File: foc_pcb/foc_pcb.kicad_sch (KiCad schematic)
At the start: 67 parts, among them IC1 AS5600-ASOT, J1 USB_C_Receptacle_USB2.0, J10 Conn_02x03_Top_Bottom, J11 Conn_01x03, J12 USB4105-GF-A, J2 Conn_01x03, J3 Conn_01x03, J4 Conn_01x04, J5 XT60PW-M, J6 XT60PW-M, J7 Conn_01x02, J8 Conn_01x02, J9 Conn_01x02, SW1 SW_Push, U1 DRV8313PWPR, U2 ATMEGA328P-AU, U3 BSS138-7-F, U4 BSS138-7-F, U5 CH340C, Y1 ABM3-16MHZ

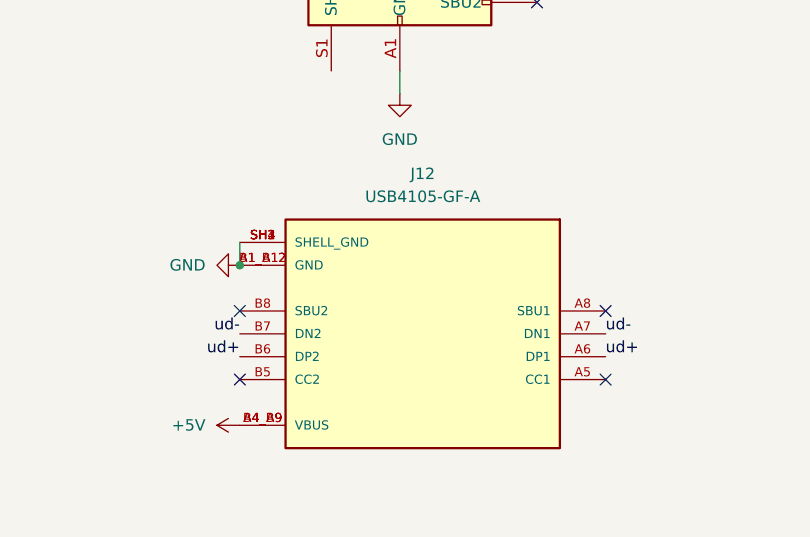
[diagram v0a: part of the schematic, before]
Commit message: reverted to old usb, pray to jlc gods
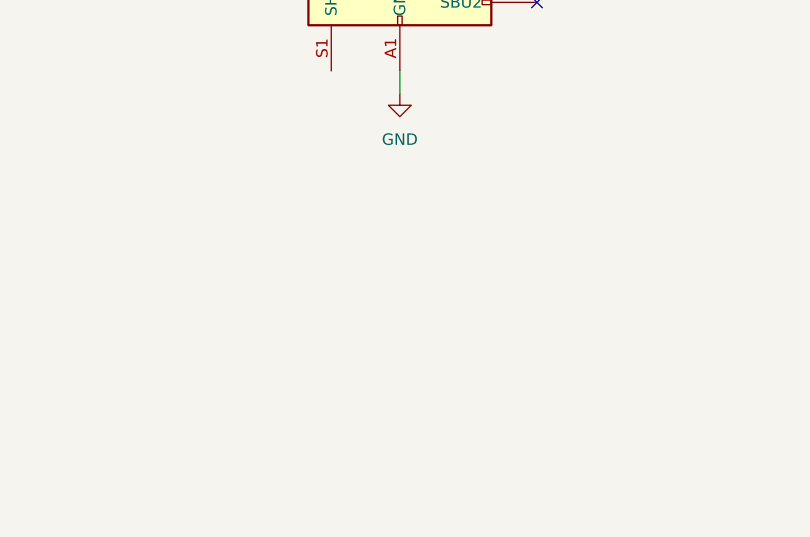
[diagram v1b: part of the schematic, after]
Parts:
- removed J12: USB4105-GF-A, USB4105-GF-A:GCT_USB4105-GF-A, symbol USB4105-GF-A:USB4105-GF-A
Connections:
- no-connect marks 14 -> 10

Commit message: board v1 done, to be ordered soon
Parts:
- removed C5: 1uF, Capacitor_SMD:C_0603_1608Metric, symbol Device:C_Polarized_US
- removed J1: USB_C_Receptacle_USB2.0, Connector_USB:USB_C_Receptacle_G-Switch_GT-USB-7010ASV, symbol Connector:USB_C_Receptacle_USB2.0
- added H10, H11, H12, H9: boardMount, MountingHole:MountingHole_3.2mm_M3, symbol Mechanical:MountingHole
- added J1: Conn_01x03, Connector_PinHeader_2.54mm:PinHeader_1x03_P2.54mm_Vertical, symbol Connector_Generic:Conn_01x03
- added J12: 10118193-0001LF, usbMicroB:AMPHENOL_10118193-0001LF, symbol 10118193-0001LF:10118193-0001LF
- C4: symbol Device:C_Polarized_US -> Device:C
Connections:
- net +5V: now also J12.1 (VUSB)
- net GND: now also J1.3 (Pin_3), J12.5 (GND)
- net uRX: now also J1.1 (Pin_1)
- net uTX: now also J1.2 (Pin_2)
- net ud+: now also J12.3 (D+)
- net ud-: now also J12.2 (D-)
- no-connect marks 10 -> 12

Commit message: readme updated
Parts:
- D1: value 19-213/Y2C-CQ2R2L/3T(CY) -> 150060RS75000
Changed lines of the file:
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@@
 			)
 		)
-		(property "Value" "19-213/Y2C-CQ2R2L/3T(CY)"
-			(at 176.53 107.95 0)
+		(property "Value" "150060RS75000"
+			(at 168.148 107.95 0)
 			(effects
 				(font

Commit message: V2 redesign done, needs review
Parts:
- removed D1: 150060RS75000, simpleFOC_led:LED0603-RD-YELLOW, symbol Device:LED
- removed D2: 1N5819HW-7-F, 1N5819HW-7-F:SOD3715X145N, symbol 1N5819HW-7-F:1N5819HW-7-F
- removed D3: LED, KT-0603R:LED0603-RD, symbol Device:LED
- removed H10, H11, H12, H9: boardMount, MountingHole:MountingHole_3.2mm_M3, symbol Mechanical:MountingHole
- removed H5, H6, H7, H8: motorMount, MountingHole:MountingHole_3.2mm_M3, symbol Mechanical:MountingHole
- removed J1, J11, J2: Conn_01x03, Connector_PinHeader_2.54mm:PinHeader_1x03_P2.54mm_Vertical, symbol Connector_Generic:Conn_01x03
- removed J4: Conn_01x04, Connector_PinHeader_2.54mm:PinHeader_1x04_P2.54mm_Vertical, symbol Connector_Generic:Conn_01x04
- removed J7: Conn_01x02, Connector_PinHeader_2.54mm:PinHeader_1x02_P2.54mm_Vertical, symbol Connector_Generic:Conn_01x02
- added D1: 1N5819HW-7-F, 1N5819HW-7-F:SOD3715X145N, symbol 1N5819HW-7-F:1N5819HW-7-F
- added J1: MPU6050, Connector_PinHeader_2.54mm:PinHeader_1x08_P2.54mm_Vertical, symbol Connector_Generic:Conn_01x08
- added U6: ~, XIAO-ESP32S3:MOUDLE14P-SMD-2.54-21X17.8MM, symbol XIAO-ESP32S3:MOUDLE-SEEEDUINO-XIAO-ESP32S3-SMD
- added U7: BSS138-7-F, BSS138-7-F:SOT95P240X110-3N, symbol BSS138-7-F:BSS138-7-F
- C11: value VT1V101M-CRE77 -> UWT1V101MCL1GS; footprint VT1V101M-CRE77:CAP-SMD_BD6.3-L6.6-W6.6-FD -> UWT1V101MCL1GS:PCAP_6.3x7.7-ELECT_NCA-L
- D5: footprint KT-0603R:LED0603-RD -> LED_SMD:LED_0603_1608Metric
- IC1: Description_1 (none) -> Hall Effect Sensor Angle External Magnet, Not Included Gull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
- J5, J6: Description_1 (none) -> Socket, DC supply, male, PIN: 2
- R4, R8: value 1k -> 10k
- U2: footprint ATMEGA328P-AU-NEW:QFP80P900X900X120-32N -> ATMEGA328P-AU:QFP80P900X900X120-32N
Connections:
- net 3vin is gone; now on net +3.3V: R15.1, R17.1, U3.1 (G), U4.1 (G)
- net aRX2 is gone; now on net GND: U2.14 (PB2)
- net +3.3V: now also R4.1, J1.1 (Pin_1), U7.1 (G)
- net +5V: now also R8.1, U5.4 (V3), VR1.2 (OUTPUT), D1.C; no longer U5.16 (VCC)
- net GND: now also J1.2 (Pin_2), U6.13 (GND)
- net VCC: no longer R4.1
- net miso: now also R18.2, U4.3 (D)
- net mosi: now also R16.2, U3.3 (D)
- net sck: now also U7.3 (D)
- net gpio_1: now reaches U2.23 (PC0)
- net gpio_2: now reaches U2.24 (PC1)
- net at C10.1, C12.2: now also U5.16 (VCC); no longer U5.4 (V3)
- net esp_sck: now reaches R4.2
- net esp_sck: now also U6.9 (PA7_A8_D8_SCK), U7.2 (S)
- removed net aRX1: R16.2, U2.12 (PB0), U3.3 (D)
- removed net aTX1: R18.2, U2.13 (PB1), U4.3 (D)
- net aTX2: no longer names the net of U2.32 (PD2)
- net escl renamed scl
- net esda renamed sda
- net lvRX renamed esp_mosi
- net esp_mosi: now also U6.11 (PA6_A10_D10_MOSI)
- net lvTX renamed esp_miso
- net esp_miso: now also U6.10 (PA5_A9_D9_MISO)
- new net: D1.A, U6.14 (5V)
- new net esp_scl_0: U6.4 (PA11_A3_D3)
- new net esp_scl_1: J1.3 (Pin_3), U6.6 (PA9_A5_D5_SCL)
- new net esp_sda_0: U6.3 (PA10_A2_D2)
- new net esp_sda_1: J1.4 (Pin_4), U6.5 (PA8_A4_D4_SDA)
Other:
- moved on the sheet: C1, C10, C11, C12, C13, C14, C16, C17, C2, C3, C4, C6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

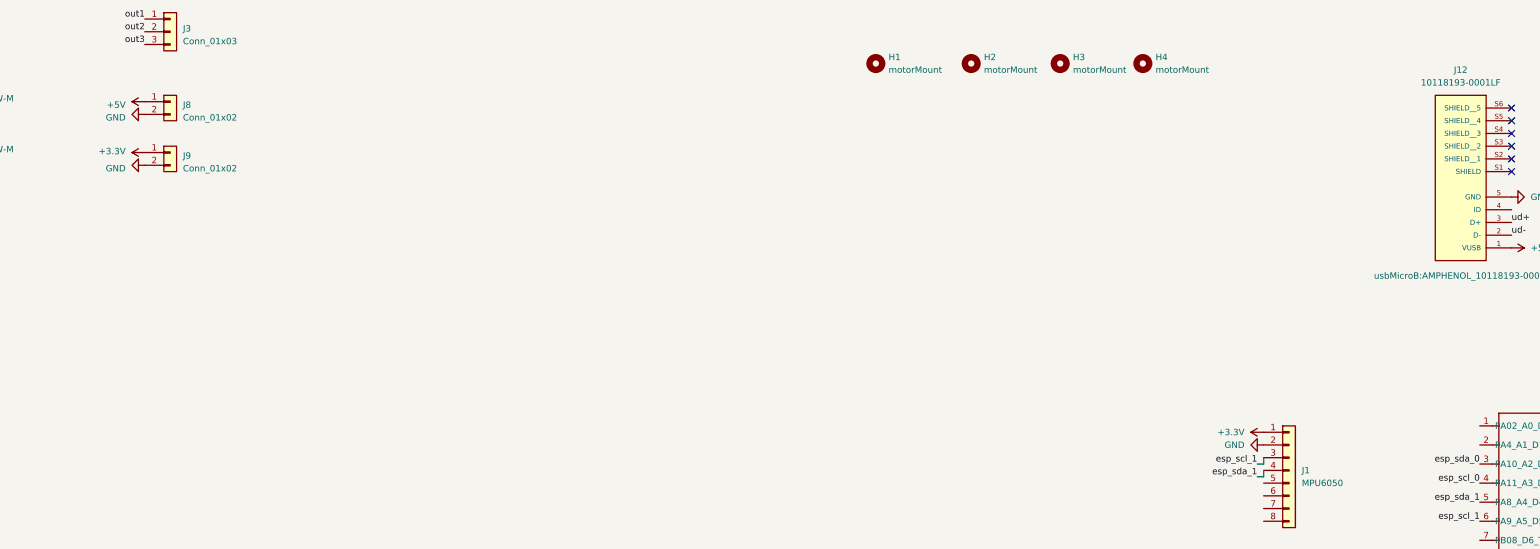
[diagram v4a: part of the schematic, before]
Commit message: compacted layout, finished V2
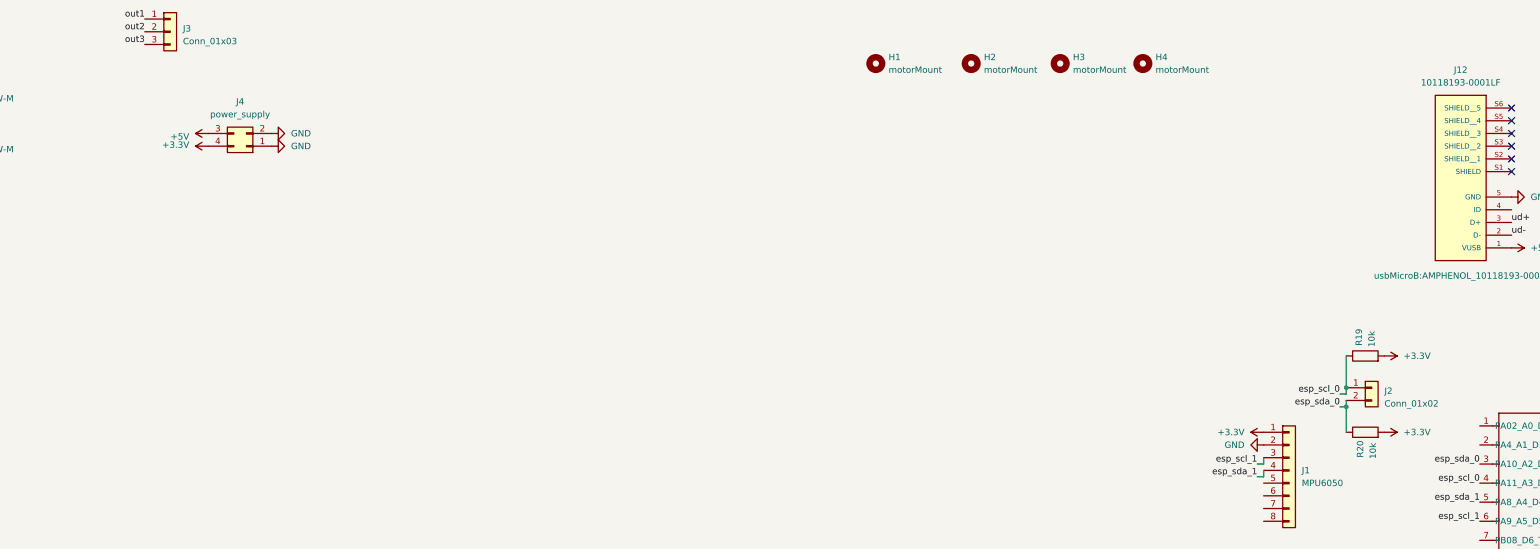
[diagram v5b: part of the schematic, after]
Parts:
- removed J8, J9: Conn_01x02, Connector_PinHeader_2.54mm:PinHeader_1x02_P2.54mm_Vertical, symbol Connector_Generic:Conn_01x02
- added J2: Conn_01x02, Connector_PinHeader_2.54mm:PinHeader_1x02_P2.54mm_Vertical, symbol Connector_Generic:Conn_01x02
- added J4: power_supply, Connector_PinHeader_2.54mm:PinHeader_2x02_P2.54mm_Vertical, symbol Connector_Generic:Conn_02x02_Counter_Clockwise
- added R19, R20: 10k, Resistor_SMD:R_0603_1608Metric, symbol Device:R
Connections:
- net +3.3V: now also J4.4 (Pin_4), R19.2, R20.2
- net +5V: now also J4.3 (Pin_3)
- net GND: now also J4.1 (Pin_1), J4.2 (Pin_2)
- net esp_scl_0: now also J2.1 (Pin_1), R19.1
- net esp_sda_0: now also J2.2 (Pin_2), R20.1
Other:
- company: VERTEX -> avaninder.com

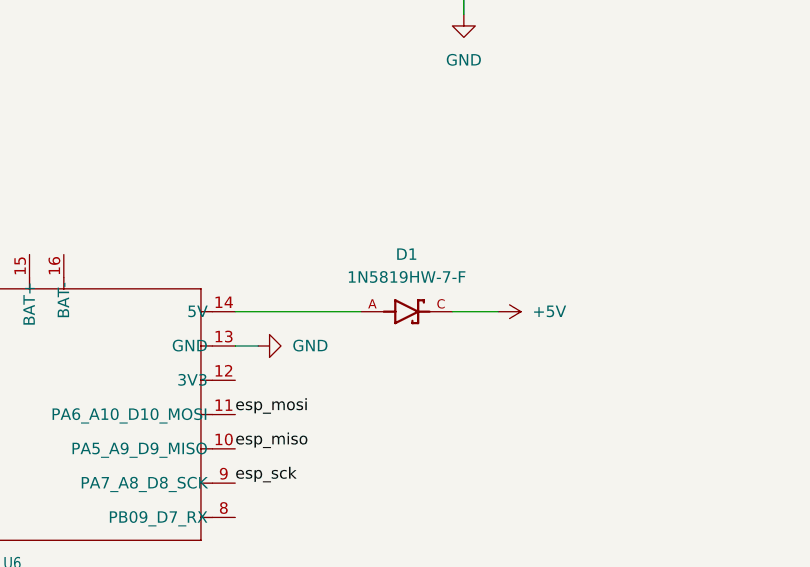
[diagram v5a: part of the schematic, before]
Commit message: added kicad preview
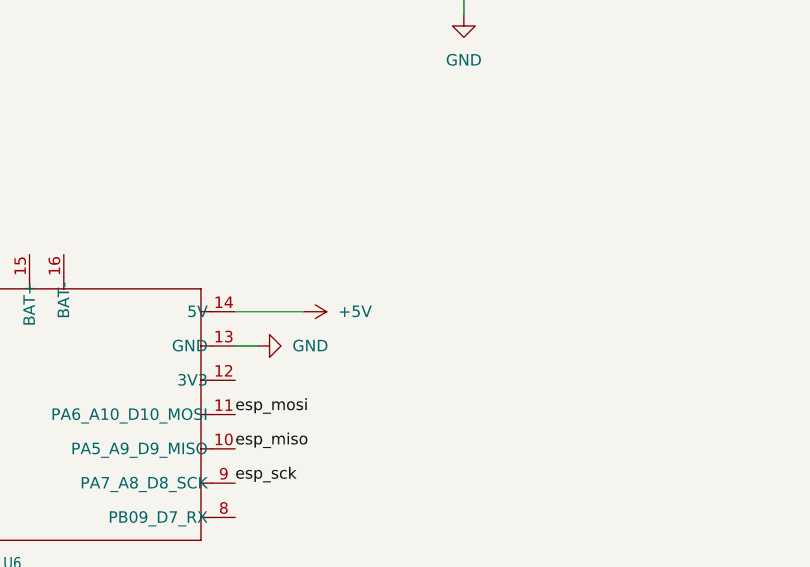
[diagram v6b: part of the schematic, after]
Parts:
- removed D1: 1N5819HW-7-F, 1N5819HW-7-F:SOD3715X145N, symbol 1N5819HW-7-F:1N5819HW-7-F
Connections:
- net +5V: now also U6.14 (5V)
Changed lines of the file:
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@@
 	(wire
 		(pts
-			(xy 441.96 219.71) (xy 447.04 219.71)
-		)
-		(stroke
-			(width 0)
-			(type default)
-		)
-	)
-	(wire
-		(pts
 			(xy 238.76 59.69) (xy 238.76 62.23)
 		)
@@
 	(wire
 		(pts
-			(xy 417.83 219.71) (xy 431.8 219.71)
+			(xy 417.83 219.71) (xy 425.45 219.71)
 		)
 		(stroke
@@
 	(symbol
 		(lib_id "power:+5V")
-		(at 447.04 219.71 270)
+		(at 425.45 219.71 270)
 		(unit 1)
 		(exclude_from_sim no)
@@
 		(fields_autoplaced yes)
 		(property "Reference" "#PWR012"
-			(at 443.23 219.71 0)
+			(at 421.64 219.71 0)
 			(effects
 				(font
@@
 		)
 		(property "Value" "+5V"
-			(at 450.85 219.7099 90)
+			(at 429.26 219.7099 90)
 			(effects
 				(font
@@
 		)
 		(property "Footprint" ""
-			(at 447.04 219.71 0)
+			(at 425.45 219.71 0)
 			(effects
 				(font
@@
 		)
 		(property "Datasheet" ""
-			(at 447.04 219.71 0)
+			(at 425.45 219.71 0)
 			(effects
 				(font
@@
 		)
 		(property "Description" "Power symbol creates a global label with name \"+5V\""
-			(at 447.04 219.71 0)
+			(at 425.45 219.71 0)
 			(effects
 				(font
@@
 					(unit 1)
 				)
-			)
-		)
-	)
-	(symbol
-		(lib_id "1N5819HW-7-F:1N5819HW-7-F")
-		(at 436.88 219.71 0)
-		(unit 1)
-		(exclude_from_sim no)
-		(in_bom yes)
-		(on_board yes)
-		(dnp no)
-		(fields_autoplaced yes)
-		(property "Reference" "D1"
-			(at 436.88 213.36 0)
-			(effects
-				(font
-					(size 1.27 1.27)
-				)
-			)
-		)
-		(property "Value" "1N5819HW-7-F"
-			(at 436.88 215.9 0)
-			(effects
-				(font
-					(size 1.27 1.27)
-				)
-			)
-		)
-		(property "Footprint" "1N5819HW-7-F:SOD3715X145N"
-			(at 436.88 219.71 0)
-			(effects
-				(font
-					(size 1.27 1.27)
-				)
-				(justify bottom)
-				(hide yes)
-			)
-		)
-		(property "Datasheet" ""
-			(at 436.88 219.71 0)
-			(effects
-				(font
-					(size 1.27 1.27)
-				)
-				(hide yes)
-			)
-		)
-		(property "Description" ""
-			(at 436.88 219.71 0)
-			(effects
-				(font
-					(size 1.27 1.27)
-				)
-				(hide yes)
-			)
-		)
-		(property "DigiKey_Part_Number" ""
-			(at 436.88 219.71 0)
-			(effects
-				(font
-					(size 1.27 1.27)
-				)
-				(justify bottom)
-				(hide yes)
-			)
-		)
-		(property "MF" "Diodes Zetex"
-			(at 436.88 219.71 0)
-			(effects
-				(font
-					(size 1.27 1.27)
-				)
-				(justify bottom)
-				(hide yes)
-			)
-		)
-		(property "Purchase-URL" "https://www.snapeda.com/api/url_track_click_mouser/?unipart_id=4796063&manufacturer=Diodes Zetex&part_name=1N5819HW-7-F&search_term=None"
-			(at 436.88 219.71 0)
-			(effects
-				(font
-					(size 1.27 1.27)
-				)
-				(justify bottom)
-				(hide yes)
-			)
-		)
-		(property "Package" "None"
-			(at 436.88 219.71 0)
-			(effects
-				(font
-					(size 1.27 1.27)
-				)
-				(justify bottom)
-				(hide yes)
-			)
-		)
-		(property "Check_prices" "https://www.snapeda.com/parts/1N5819HW-7-F/Zetex/view-part/?ref=eda"
-			(at 436.88 219.71 0)
-			(effects
-				(font
-					(size 1.27 1.27)
-				)
-				(justify bottom)
-				(hide yes)
-			)
-		)
-		(property "STANDARD" "IPC-7351B"
-			(at 436.88 219.71 0)
-			(effects
-				(font
-					(size 1.27 1.27)
-				)
-				(justify bottom)
-				(hide yes)
-			)
-		)
-		(property "PARTREV" "18-2"
-			(at 436.88 219.71 0)
-			(effects
-				(font
-					(size 1.27 1.27)
-				)
-				(justify bottom)
-				(hide yes)
-			)
-		)
-		(property "SnapEDA_Link" "https://www.snapeda.com/parts/1N5819HW-7-F/Zetex/view-part/?ref=snap"
-			(at 436.88 219.71 0)
-			(effects
-				(font
-					(size 1.27 1.27)
-				)
-				(justify bottom)
-				(hide yes)
-			)
-		)
-		(property "MP" "1N5819HW-7-F"
-			(at 436.88 219.71 0)
-			(effects
-				(font
-					(size 1.27 1.27)
-				)
-				(justify bottom)
-				(hide yes)
-			)
-		)
-		(property "Description_1" "\nDiode Schottky 40V 1A 2-Pin SOD-123 T/R\n"
-			(at 436.88 219.71 0)
-			(effects
-				(font
-					(size 1.27 1.27)
-				)
-				(justify bottom)
-				(hide yes)
-			)
-		)
-		(property "MANUFACTURER" "Diodes Inc."
-			(at 436.88 219.71 0)
-			(effects
-				(font
-					(size 1.27 1.27)
-				)
-				(justify bottom)
-				(hide yes)
-			)
-		)
-		(pin "A"
-		)
-		(pin "C"
-		)
-		(instances
-			(project ""
-				(path "/f8f15c75-e6d6-45a2-af6e-ae3d4a1b02ab"
-					(reference "D1")
-					(unit 1)
-				)

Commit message: V3 Intial Commit
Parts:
- removed C10: 1nF, Capacitor_SMD:C_0603_1608Metric, symbol Device:C
- removed C12: 10nF, Capacitor_SMD:C_0603_1608Metric, symbol Device:C
- removed C16, C17: 22pF, Capacitor_SMD:C_0603_1608Metric, symbol Device:C
- removed C6, C7, C8, C9: 100nF, Capacitor_SMD:C_0603_1608Metric, symbol Device:C
- removed J1: MPU6050, Connector_PinHeader_2.54mm:PinHeader_1x08_P2.54mm_Vertical, symbol Connector_Generic:Conn_01x08
- removed J10: Conn_02x03_Top_Bottom, Connector_PinHeader_2.54mm:PinHeader_2x03_P2.54mm_Vertical, symbol Connector_Generic:Conn_02x03_Top_Bottom
- removed J12: 10118193-0001LF, usbMicroB:AMPHENOL_10118193-0001LF, symbol 10118193-0001LF:10118193-0001LF
- removed J5, J6: XT60PW-M, XT60PW-M:AMASS_XT60PW-M, symbol XT60PW-M:XT60PW-M
- removed R12, R15, R16, R17, R18, R19, R20, R8: 10k, Resistor_SMD:R_0603_1608Metric, symbol Device:R
- removed R7: 1k, Resistor_SMD:R_0603_1608Metric, symbol Device:R
- removed SW1: SW_Push, YTS-A011-2B:SW-SMD_L4.0-W3.0-LS4.6, symbol Switch:SW_Push
- removed U2: ATMEGA328P-AU, ATMEGA328P-AU:QFP80P900X900X120-32N, symbol ATMEGA328P-AU:ATMEGA328P-AU
- removed U3, U4, U7: BSS138-7-F, BSS138-7-F:SOT95P240X110-3N, symbol BSS138-7-F:BSS138-7-F
- removed U5: CH340C, Package_SO:SOIC-16_3.9x9.9mm_P1.27mm, symbol Interface_USB:CH340C
- removed Y1: ABM3-16MHZ, ABM3-16.000MHZ-B2-T:XTAL_ABM3-16.000MHZ-B2-T, symbol ABM3-16.000MHZ-B2-T:ABM3-16.000MHZ-B2-T
- added D1: 1N5819HW-7-F, 1N5819HW-7-F:SOD3715X145N, symbol 1N5819HW-7-F:1N5819HW-7-F
- added J1: IMU, Connector_PinHeader_2.00mm:PinHeader_1x04_P2.00mm_Vertical, symbol Connector_Generic:Conn_01x04
- added J5: ESP, Connector_PinHeader_2.00mm:PinHeader_1x04_P2.00mm_Vertical, symbol Connector_Generic:Conn_01x04
- added JP1: esp_diode_skip, Jumper:SolderJumper-2_P1.3mm_Open_TrianglePad1.0x1.5mm, symbol Jumper:SolderJumper_2_Open
- added JP2: pullup_scl, Jumper:SolderJumper-2_P1.3mm_Open_TrianglePad1.0x1.5mm, symbol Jumper:SolderJumper_2_Open
- added JP3: pullup_sda, Jumper:SolderJumper-2_P1.3mm_Open_TrianglePad1.0x1.5mm, symbol Jumper:SolderJumper_2_Open
- added JP4: 3V3 DRV, Jumper:SolderJumper-2_P1.3mm_Open_TrianglePad1.0x1.5mm, symbol Jumper:SolderJumper_2_Open
- added JP5: 3V3 ESP, Jumper:SolderJumper-2_P1.3mm_Open_TrianglePad1.0x1.5mm, symbol Jumper:SolderJumper_2_Open
- J2: value Conn_01x02 -> BATT_IN; footprint Connector_PinHeader_2.54mm:PinHeader_1x02_P2.54mm_Vertical -> Connector_JST:JST_VH_B2P-VH_1x02_P3.96mm_Vertical
- R11, R9: value 4.7k -> 1k
- R5: value 10k -> 4.7k
- R6: value 1k -> 4.7k
- renumbered U6 to U2
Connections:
- net esp_miso is gone; now on net esp_sda: U2.10 (PA5_A9_D9_MISO)
- net esp_scl_1 is gone; now on net scl: U2.6 (PA9_A5_D5_SCL)
- net esp_sda_1 is gone; now on net sda: U2.5 (PA8_A4_D4_SDA)
- net uRX is gone; now on net +3.3V: R6.2
- net +3.3V: now also C13.1, C14.1, IC1.1 (VDD5V), IC1.2 (VDD3V3), R11.1, R5.2, R9.1, J1.2 (Pin_2), JP4.1 (A), JP5.2 (B); no longer C1.2, R1.2, R2.2, R3.2, R4.1, U1.15 (V3P3)
- net +5V: now also D1.A, JP1.2 (B); no longer C13.1, IC1.1 (VDD5V), R11.1, R5.2, R9.1, U2.14 (5V)
- net GND: now also J2.1 (Pin_1), J1.1 (Pin_1), J5.1 (Pin_1)
- net VCC: now also J2.2 (Pin_2)
- net en: now also R4.1, U2.1 (PA02_A0_D0); no longer U1.22 (EN3), U1.24 (EN2), U1.26 (EN1)
- net in1: now also U2.2 (PA4_A1_D1)
- net in2: now also U2.3 (PA10_A2_D2)
- net in3: now also U2.4 (PA11_A3_D3)
- net scl: now also J1.4 (Pin_4), JP2.1 (A); no longer R9.2
- net sda: now also J1.3 (Pin_3), JP3.1 (A); no longer R11.2
- net at U2.12 (3V3): now also JP5.1 (A)
- net esp_sda: now reaches R6.1
- net esp_sda: now also J5.3 (Pin_3)
- net esp_mosi: no longer names the net of U2.11 (PA6_A10_D10_MOSI)
- net esp_sck: no longer names the net of R4.2
- net esp_sck: now also U1.22 (EN3), U1.24 (EN2), U1.26 (EN1); no longer U2.9 (PA7_A8_D8_SCK)
- removed net esp_scl_0: J2.1 (Pin_1), U2.4 (PA11_A3_D3)
- removed net esp_sda_0: J2.2 (Pin_2), U2.3 (PA10_A2_D2)
- net rst renamed esp_scl
- net esp_scl: now also U2.9 (PA7_A8_D8_SCK), J5.4 (Pin_4)
- new net: JP3.2 (B), R11.2
- new net: D1.C, JP1.1 (A), U2.14 (5V)
- new net: JP2.2 (B), R9.2
- new net v3p3: C1.2, JP4.2 (B), R1.2, R2.2, R3.2, U1.15 (V3P3)
- no-connect marks 12 -> 0
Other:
- moved on the sheet: C1, C11, C13, C14, C2, C3, C4, D5, H1, H2, H3, H4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
